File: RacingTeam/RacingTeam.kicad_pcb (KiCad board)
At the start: 0 parts

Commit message: Update FUSE_0154004.DRTL.kicad_mod, GRC2022.mod, and 15 more files...
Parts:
- added C1: 10nF, GRC2022:C_0603, F.Cu at (200.0, 57.5)
- added C2: 0.1uF, GRC2022:C_0603, F.Cu at (199.5, 65.1)
- added C3: 10nF, GRC2022:C_0603, F.Cu at (185.0, 78.1)
- added C4: 0.1uF, GRC2022:C_0603, F.Cu at (191.9, 74.0)
- added C5: 100nF, GRC2022:C_0603, F.Cu at (197.5, 118.0)
- added C6: 100nF, GRC2022:C_0603, F.Cu at (184.4, 120.5)
- added C7: C7, GRC2022:C_0603, F.Cu at (166.0, 110.9)
- added C8: 1μF, GRC2022:C_0603, F.Cu at (190.0, 120.0)
- added D1: 12V, GRC2022:SOD57-10, Cmts.User at (207.0, 45.0)
- added D2: 12V, GRC2022:SOD57-10, Cmts.User at (174.0, 68.5)
- added D3: Flyback, GRC2022:SD0805S040S0R5, F.Cu at (214.0, 77.0)
- added D4: Flyback, GRC2022:SD0805S040S0R5, F.Cu at (214.5, 49.5)
- added D5: Flyback, GRC2022:SD0805S040S0R5, F.Cu at (144.7, 72.7)
- added D6: LED, GRC2022:SunLED, F.Cu at (208.5, 119.5)
- added D7: D, GRC2022:SD0805S040S0R5, F.Cu at (178.5, 106.0)
- added D8: LED, GRC2022:SunLED, F.Cu at (225.5, 107.0)
- added F1: Fuse_Small, GRC2022:FUSE_0154004.DRTL, F.Cu at (157.8, 70.5)
- added F2: Fuse_Small, GRC2022:FUSE_0154004.DRTL, F.Cu at (167.0, 82.0)
- added F3: Fuse_Small, GRC2022:FUSE_0154004.DRTL, F.Cu at (169.2, 106.0)
- added F5: Fuse_Small, GRC2022:FUSE_0154004.DRTL, F.Cu at (184.8, 60.5)
- added F6: Fuse_Small, GRC2022:FUSE_0154004.DRTL, F.Cu at (191.0, 49.5)
- added J1: BusIn, GRC2022:TE_8PCV-02-006, F.Cu at (150.3, 46.8)
- added J2: Conn_01x01, GRC2022:SinglePinHeader, F.Cu at (189.5, 69.5)
- added J3: Conn_01x01, GRC2022:SinglePinHeader, F.Cu at (194.0, 42.0)
- added J4: Conn_01x01, GRC2022:SinglePinHeader, F.Cu at (178.4, 75.8)
- added J5: Conn_01x01, GRC2022:SinglePinHeader, F.Cu at (162.0, 62.5)
- added J6: PreCharge Relay Out, GRC2022:CUI_TBL001-500-02GY-2GY, Cmts.User at (222.0, 74.2)
- added J7: AIROut, GRC2022:CUI_TBL001-500-02GY-2GY, Cmts.User at (222.0, 53.4)
- added J8: Discharge Relay Out, GRC2022:CUI_TBL001-500-02GY-2GY, Cmts.User at (138.5, 68.5)
- added J9: PCB OUT, GRC2022:Molex, F.Cu at (224.0, 118.0)
- added JP1: Jumper, GRC2022:DualPinHeader, F.Cu at (213.0, 117.0)
- added JP2: Jumper, GRC2022:DualPinHeader, F.Cu at (219.0, 110.0)
- added PS1: EC3SAW-24S12P, GRC2022:EC3SAW-24S12P, F.Cu at (134.0, 91.0)
- added Q1: TP0610T, GRC2022:SOT95P280X100-6N, F.Cu at (208.0, 64.5)
- added Q2: 2N7002, GRC2022:TRANS_MMBT2907A, F.Cu at (215.0, 61.0)
- added Q3: 2N7002, GRC2022:TRANS_MMBT2907A, F.Cu at (131.0, 58.5)
- added Q4: 2N7002, GRC2022:TRANS_MMBT2907A, F.Cu at (139.5, 58.5)
- added Q5: 2N7002, GRC2022:TRANS_MMBT2907A, F.Cu at (196.5, 104.5)
- added Q6: TP0610T, GRC2022:SOT95P280X100-6N, F.Cu at (207.5, 109.0)
- added Q7: 2N7002, GRC2022:TRANS_MMBT2907A, F.Cu at (187.3, 105.7)
- added Q8: TP0610T, GRC2022:SOT95P280X100-6N, F.Cu at (219.5, 104.5)
- added R1: 1.3kΩ, GRC2022:R_0603, F.Cu at (152.0, 78.7)
- added R10: 150kOhm, GRC2022:R_0805, F.Cu at (180.5, 49.5)
- added R11: 4kOhm, GRC2022:R_0805, F.Cu at (181.5, 44.0)
- added R12: 249kΩ, GRC2022:R_0805, F.Cu at (158.5, 56.5)
- added R13: 249kΩ, GRC2022:R_0805, F.Cu at (153.3, 58.6)
- added R14: 249kΩ, GRC2022:R_0805, F.Cu at (152.5, 64.9)
- added R15: 49kΩ, GRC2022:R_0805, F.Cu at (146.5, 63.9)
- added R16: 100Ω, GRC2022:R_0603, F.Cu at (195.0, 55.0)
- added R17: 100Ω, GRC2022:R_0603, F.Cu at (194.9, 60.5)
- added R18: 100Ω, GRC2022:R_0603, F.Cu at (168.8, 75.7)
- added R19: 100Ω, GRC2022:R_0603, F.Cu at (178.2, 83.1)
- added R2: 1.3kΩ, GRC2022:R_0603, F.Cu at (157.0, 77.2)
- added R20: 22kΩ, GRC2022:R_0603, F.Cu at (205.5, 52.0)
- added R21: 0Ω, GRC2022:R_0603, F.Cu at (209.5, 70.6)
- added R22: 22kΩ, GRC2022:R_0603, F.Cu at (199.0, 75.9)
- added R23: 0Ω, GRC2022:R_0603, F.Cu at (214.6, 55.6)
- added R24: 1.2kΩ, GRC2022:R_0603, F.Cu at (200.0, 80.5)
- added R25: 0Ω, GRC2022:R_0603, F.Cu at (148.4, 76.1)
- added R26: 10kΩ, GRC2022:R_0603, F.Cu at (201.0, 104.5)
- added R27: 22kΩ, GRC2022:R_0603, F.Cu at (180.7, 118.0)
- added R28: 499Ω, GRC2022:R_0603, F.Cu at (204.0, 118.5)
- added R29: 22kΩ, GRC2022:R_0603, F.Cu at (184.9, 117.5)
- added R3: 1.3kΩ, GRC2022:R_0603, F.Cu at (157.0, 82.4)
- added R30: 220kΩ, GRC2022:R_0603, F.Cu at (190.0, 114.5)
- added R31: 10kΩ, GRC2022:R_0603, F.Cu at (214.5, 104.0)
- added R32: 499Ω, GRC2022:R_0603, F.Cu at (229.1, 104.0)
- added R4: 4.7kΩ, GRC2022:R_0603, F.Cu at (171.5, 56.1)
- added R5: 6.8kΩ, GRC2022:R_0603, F.Cu at (171.5, 62.1)
- added R6: 249kΩ, GRC2022:R_0805, F.Cu at (164.5, 56.5)
- added R7: 22kΩ, GRC2022:R_0805, Cmts.User at (146.5, 58.4)
- added R8: 150kOhm, GRC2022:R_0805, F.Cu at (168.0, 49.5)
- added R9: 150kOhm, GRC2022:R_0805, F.Cu at (174.0, 49.5)
- added U1: LM311, GRC2022:SOP65P640X120-8N, F.Cu at (207.5, 57.5)
- added U2: LM311, GRC2022:SOP65P640X120-8N, F.Cu at (192.0, 78.0)
- added U3: 4N35, GRC2022:OPTO_4N35SM, F.Cu at (199.0, 92.5)
- added U6: NE555D, GRC2022:NE555PSRE4, F.Cu at (197.5, 112.5)
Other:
- board outline added: 104 x 92 mm
- copper layers 0 -> 4
- net class Default added: clearance 0.2, trace_width 0.25, via_dia 0.8, via_drill 0.4

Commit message: Update FSAELogo.kicad_mod, GRC2022.mod, and 11 more files...
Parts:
- removed C7: C7, GRC2022:C_0603
- added G***: LOGO, Footprints:PCB, F.Cu at (198.8, 103.6)
- added G***: LOGO, Footprints:UofGLogo, F.Cu at (183.8, 93.0)
- added G***: LOGO, Footprints:HVLogo, F.Cu at (202.0, 65.5)
- added J10: BatteryIn, GRC2022:CUI_TBL001-500-02GY-2GY, F.Cu at (113.0, 51.4)
- added J11: ShutdownIn, GRC2022:CUI_TBL001-500-02GY-2GY, F.Cu at (160.2, 119.4)
- D1, D2, J6, J7, J8, R7: moved to F.Cu
- moved J9 109.3 mm to (115.0, 109.5), turned to 270 degrees
- moved R32 95.0 mm to (135.1, 118.0)
- moved D8 94.8 mm to (131.2, 117.0), turned to 90 degrees
- moved JP2 92.3 mm to (126.8, 113.5), turned to 0 degrees
- moved JP1 86.8 mm to (126.8, 107.3), turned to 180 degrees
- moved Q8 84.7 mm to (135.2, 112.8), turned to 270 degrees
- moved D6 78.5 mm to (131.2, 105.8), turned to 90 degrees
- moved R31 71.0 mm to (144.4, 115.4), turned to 180 degrees
- moved R28 69.9 mm to (135.1, 106.8), turned to 180 degrees
- moved Q6 65.9 mm to (142.0, 101.8)
- moved D7 49.9 mm to (130.5, 92.2), turned to 0 degrees
- moved Q5 48.1 mm to (149.6, 93.8)
- moved R26 48.0 mm to (154.2, 93.8)
- moved U6 43.9 mm to (155.5, 99.8), turned to 0 degrees
- moved C5 43.8 mm to (161.8, 92.6), turned to 180 degrees
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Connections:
- C5 pad 2: Shutdown- -> GLV+
- C6 pad 2: Shutdown- -> GLV+
- C8 pad 2: Shutdown- -> GLV+
- D7 pad 1: Shutdown- -> GLV+
- PS1 pad 7: Shutdown- -> GLV+
- Q5 pad 1: Shutdown- -> GLV+
- Q6 pad 3: Shutdown- -> GLV+
- Q7 pad 1: Shutdown- -> GLV+
- Q8 pad 3: Shutdown- -> GLV+
- R26 pad 2: Shutdown- -> GLV+
- R28 pad 2: Shutdown- -> GLV+
- R31 pad 1: Shutdown- -> GLV+
- R32 pad 2: Shutdown- -> GLV+
- U6 pad 1: Shutdown- -> GLV+
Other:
- board size 104 x 92 mm -> 122.5 x 92.5 mm
- board text added: "12V+"
- board text added: "BatteryIn"
- board text added: "DischargeControl"
- board text added: "GND"
- board text added: "GRC 2022 Tractive System PCB"
- board text added: "Line"
- board text added: "Return"
- board text added: "ShutdownIn"
- board text added: "TSALOut"
- board text added: "Version 1.0"

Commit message: Update RacingTeam.kicad_pcb and RacingTeam.kicad_pcb-bak
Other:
- board text added: "GLV"
- board text added: "HV"

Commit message: Update RacingTeam.kicad_pcb, RacingTeam.kicad_pcb-bak, and 3 more files...
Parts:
- moved D3 5.98 mm to (212.0, 50.9), turned to 270 degrees
- moved D4 5.06 mm to (210.4, 44.0), turned to 270 degrees
- moved R21 1.93 mm to (208.9, 52.8), turned to 90 degrees
- moved Q4 1.60 mm to (129.2, 36.5), turned to 180 degrees
- moved C4 1.58 mm to (176.7, 67.1), turned to 0 degrees
- moved R23 1.57 mm to (206.4, 48.8)
- moved R11 1.25 mm to (170.5, 39.8), turned to 180 degrees
- moved R25 0.89 mm to (131.5, 46.5), turned to 180 degrees
- moved D2 0.75 mm to (154.8, 62.2)
- moved R14 0.75 mm to (137.0, 65.5)
- moved Q3 0.54 mm to (120.9, 36.4), turned to 180 degrees
- moved R4 0.53 mm to (164.8, 55.5)
- moved J2 0.50 mm to (178.5, 51.0)
- moved R5 0.34 mm to (170.2, 56.5)
- moved C1 0.25 mm to (186.5, 50.1)
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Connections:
- net Net-(C8-Pad1) renamed /555Trigger
- net Net-(D3-Pad2) renamed /PrechargeRelayOut
- net Net-(D4-Pad2) renamed /AIROut
- net Net-(D6-Pad1) renamed /OBLEDResistorGreen
- net Net-(D6-Pad2) renamed /OBLEDGreen
- net Net-(D8-Pad1) renamed /OBLEDResistorRed
- net Net-(D8-Pad2) renamed /OBLEDRed
- net Net-(F1-Pad2) renamed /TSALRef
- net Net-(F3-Pad2) renamed /Ec3Out+
- net Net-(Q5-Pad3) renamed /555Reset
- net Net-(Q7-Pad2) renamed /555Ouput
- net Net-(Q7-Pad3) renamed /555Drive
- net Net-(R29-Pad2) renamed /555DischargePullup
- D1 pad 1: /PrechargeTP+ -> /PrechargeRef
- D5 pad 1: Net-(D5-Pad1) -> /DischargeIn
- D5 pad 2: Net-(D5-Pad2) -> /DischargeOut
- F2 pad 1: /TSALREF -> /TSALCommon
- F2 pad 2: Net-(F2-Pad2) -> /TSALREF
- F6 pad 1: /PrechargeTP+ -> /PrechargeRef
- F6 pad 2: /PrechargeTP+ -> /PrechargeRef
- J3 pad 1: /PrechargeTP+ -> /PrechargeRef
- J4 pad 1: /TSALREF -> /TSALCommon
- J8 pad 1: Net-(D5-Pad1) -> /DischargeOut
- J8 pad 2: Net-(D5-Pad2) -> /DischargeIn
- Q3 pad 1: Net-(D5-Pad1) -> /DischargeIn
- Q4 pad 1: Net-(D5-Pad1) -> /DischargeIn
- R1 pad 1: Net-(F2-Pad2) -> /TSALREF
- R10 pad 2: /PrechargeTP+ -> /PrechargeRef
- R11 pad 1: /PrechargeTP+ -> /PrechargeRef
- R16 pad 2: /PrechargeTP+ -> /PrechargeRef
- R19 pad 2: /TSALREF -> /TSALCommon
- R2 pad 2: Net-(F2-Pad2) -> /TSALREF
- R25 pad 2: Net-(D5-Pad2) -> /DischargeOut
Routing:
- net AIROn: track 0.00 -> 108.6 mm, vias 0 -> 2
- net PreChargeOn: track 0.00 -> 107.1 mm, vias 0 -> 2
- net /DischargeIn: track 0.00 -> 44.3 mm
- net /PrechargeRef: track 0.00 -> 40.9 mm
- net /DischargeOut: track 0.00 -> 37.9 mm
- net BusReturn: track 0.00 -> 37.3 mm
- net GND: track 0.00 -> 29.5 mm, vias 0 -> 8
- net /PrechargeRelayOut: track 0.00 -> 25.5 mm
- net /TSALBus: track 0.00 -> 25.0 mm
- net /AIROut: track 0.00 -> 24.9 mm
- net /TSALREF: track 0.00 -> 19.1 mm
- net +12V: track 0.00 -> 18.9 mm, vias 0 -> 9
- net /CompOut: track 0.00 -> 18.8 mm
- net BusLine: track 0.00 -> 16.7 mm
- net /LM311V+: track 0.00 -> 14.5 mm
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- added copper zone on PWR, net +12V
- added copper zone on F.Cu, net BusLine
- added copper zone on F.Cu, net BusReturn
- added copper zone on PWR, net GLV+
- added copper zone on GND, net GND
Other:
- net class Default: trace_width 0.25 -> 0.4; via_dia 0.8 -> 0.4; via_drill 0.4 -> 0.3
- net class HV added: clearance 0.5, trace_width 1, via_dia 1, via_drill 0.5
- net class Large added: clearance 0.4, trace_width 0.6, via_dia 0.4, via_drill 0.3
- net class Small added: clearance 0.1, trace_width 0.25, via_dia 0.4, via_drill 0.3

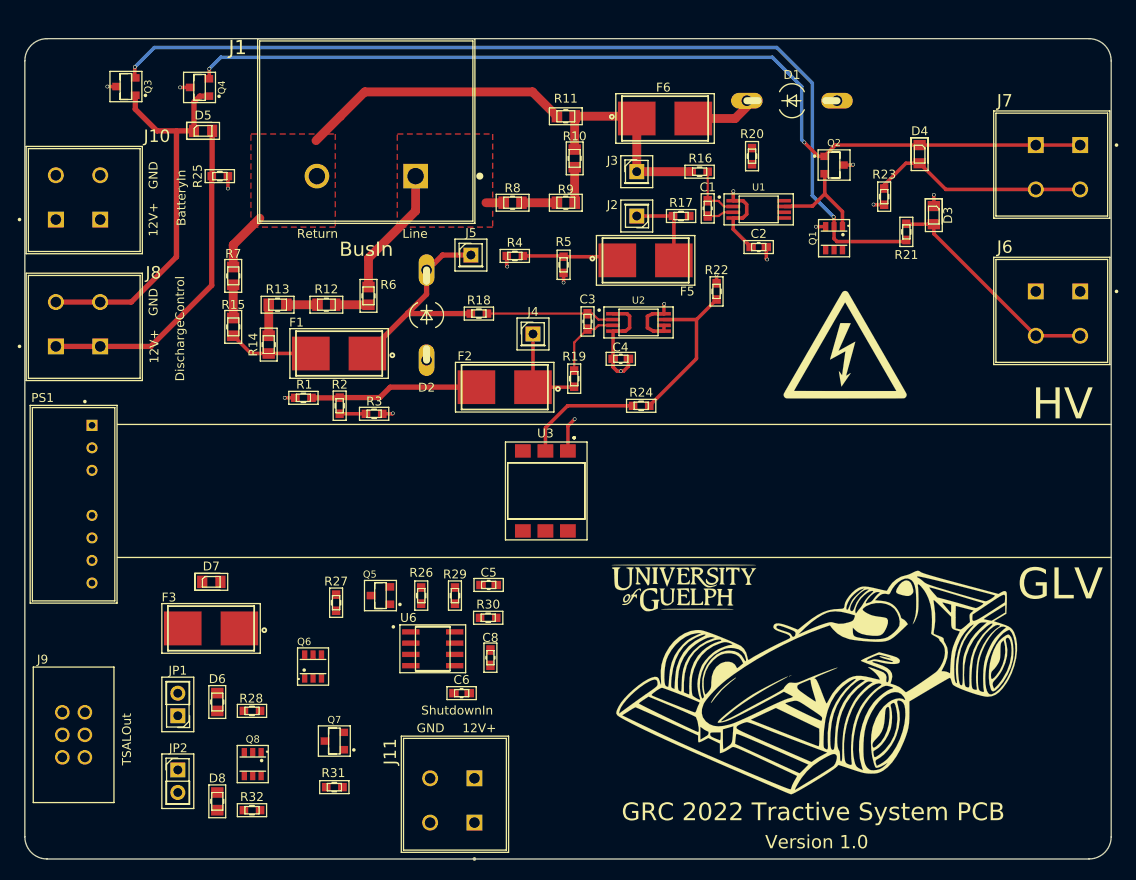
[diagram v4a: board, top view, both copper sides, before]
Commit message: Update RacingTeamPCB.dcm, RacingTeamPCB.lib, and 6 more files...
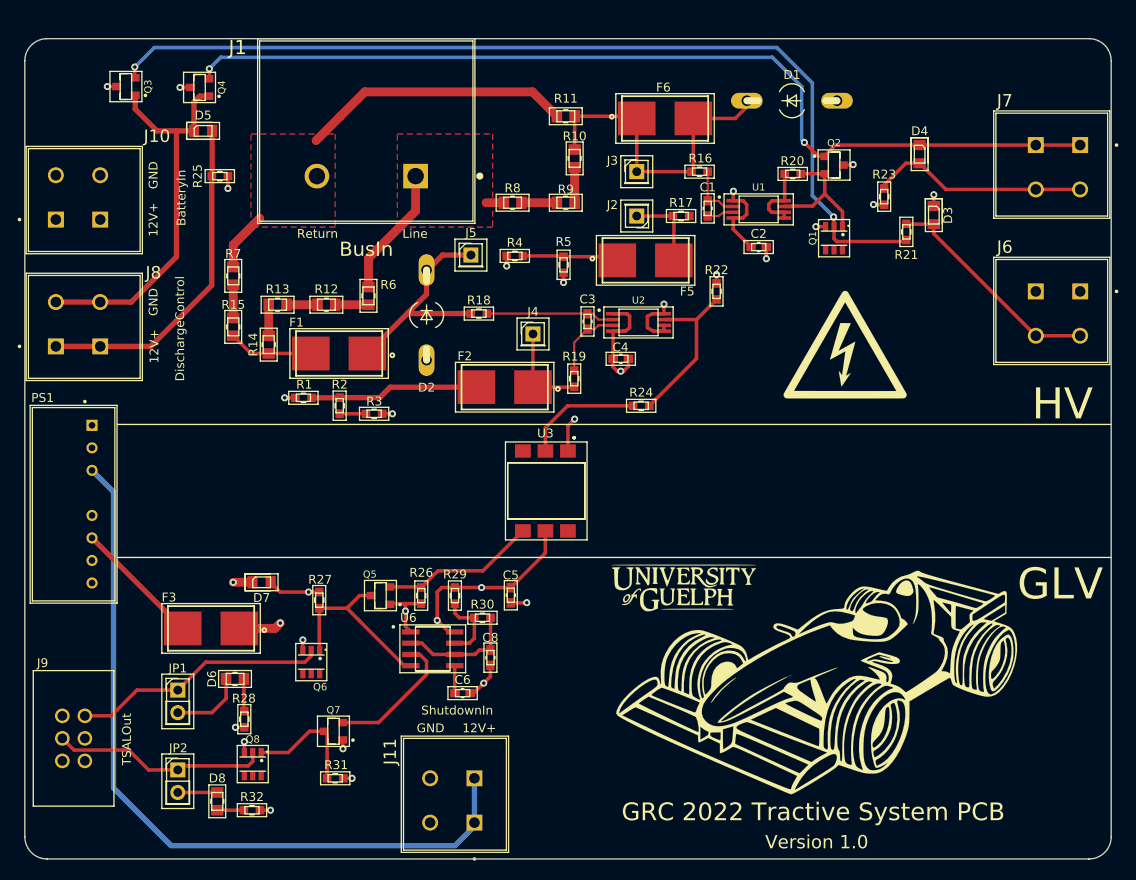
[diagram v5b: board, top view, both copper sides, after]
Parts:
- moved D7 5.68 mm to (136.2, 92.3)
- moved R20 5.00 mm to (196.1, 46.2), turned to 180 degrees
- moved D6 3.28 mm to (133.2, 103.2), turned to 180 degrees
- moved JP1 2.89 mm to (126.8, 104.5), turned to 0 degrees
- moved C5 2.76 mm to (164.3, 93.8), turned to 270 degrees
- moved R27 1.92 mm to (142.7, 94.3), turned to 270 degrees
- moved R28 1.27 mm to (134.2, 107.7), turned to 270 degrees
- moved Q7 1.10 mm to (144.3, 109.1)
- moved R31 1.00 mm to (144.5, 114.4)
- moved R30 0.65 mm to (161.1, 96.3)
- moved Q6 0.54 mm to (141.8, 101.3), turned to 270 degrees
- moved J9 0.40 mm to (115.0, 109.9)
- moved C6 0.11 mm to (158.9, 104.8)
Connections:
- net Net-(Q5-Pad2) renamed /InvertBus
- C5 pad 2: GLV+ -> GLV-
- C6 pad 2: GLV+ -> GLV-
- C8 pad 2: GLV+ -> GLV-
- D1 pad 1: /PrechargeRef -> /PrechargeRef1
- F5 pad 1: /PrechargeRef -> /PrechargeRef2
- F6 pad 1: /PrechargeRef -> /PrechargeRef1
- F6 pad 2: /PrechargeRef -> /PrechargeRef1
- J11 pad 2: GLV+ -> GLV-
- J3 pad 1: /PrechargeRef -> /PrechargeRef1
- PS1 pad 7: GLV+ -> GLV-
- Q5 pad 1: GLV+ -> GLV-
- Q7 pad 1: GLV+ -> GLV-
- R10 pad 2: /PrechargeRef -> /PrechargeRef1
- R11 pad 1: /PrechargeRef -> /PrechargeRef1
- R16 pad 2: /PrechargeRef -> /PrechargeRef1
- R26 pad 2: GLV+ -> GLV-
- R28 pad 2: GLV+ -> GLV-
- R32 pad 2: GLV+ -> GLV-
- R4 pad 2: /PrechargeRef -> /PrechargeRef2
- R5 pad 1: /PrechargeRef -> /PrechargeRef2
- U6 pad 1: GLV+ -> GLV-
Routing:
- net Shutdown+: track 0.00 -> 86.5 mm
- net /PrechargeRef: track 40.9 -> 0.00 mm
- net /PrechargeRef1: track 0.00 -> 36.1 mm
- net VCC: track 0.00 -> 33.1 mm, vias 0 -> 4
- net Green+: track 0.00 -> 28.9 mm
- net RED+: track 0.00 -> 24.3 mm
- net /555Reset: track 0.00 -> 21.1 mm
- net /InvertBus: track 0.00 -> 17.7 mm
- net GLV-: track 0.00 -> 16.3 mm, vias 0 -> 6
- net /555Ouput: track 0.00 -> 15.3 mm
- net /Ec3Out+: track 0.00 -> 14.5 mm
- net /555Drive: track 0.00 -> 13.5 mm
- net /555Trigger: track 0.00 -> 13.3 mm
- net /PrechargeRef2: track 0.00 -> 10.9 mm
- net /OBLEDGreen: track 0.00 -> 8.31 mm
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- added copper zone on GND, net GLV-
- added copper zone on PWR, net VCC
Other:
- net class Default: via_dia 0.4 -> 0.8; via_drill 0.3 -> 0.4
- net class HV: via_dia 1 -> 0.8; via_drill 0.5 -> 0.4
- net class Large: via_dia 0.4 -> 0.8; via_drill 0.3 -> 0.4
- net class Small: via_dia 0.4 -> 0.8; via_drill 0.3 -> 0.4

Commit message: Update PCBBom.xlsx, RacingTeam.kicad_pcb, and 4 more files...
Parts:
- turned PS1 to 90 degrees
